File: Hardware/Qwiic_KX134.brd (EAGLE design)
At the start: 25.4 x 25.4 mm, 62 parts, among them J2 QWIIC, J4 QWIIC, U1 KX134

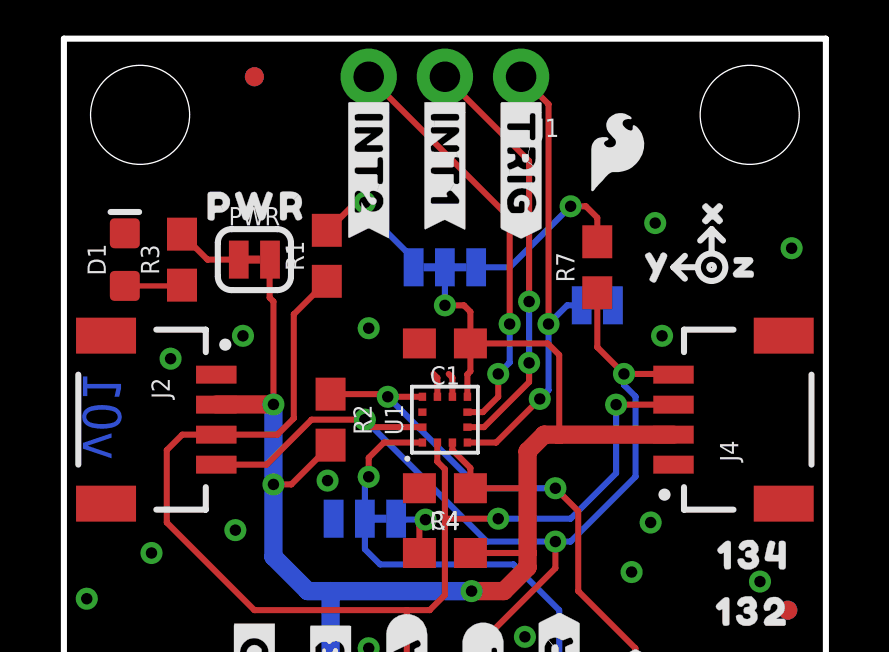
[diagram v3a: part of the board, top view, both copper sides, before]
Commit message: updating version number and orientation for review
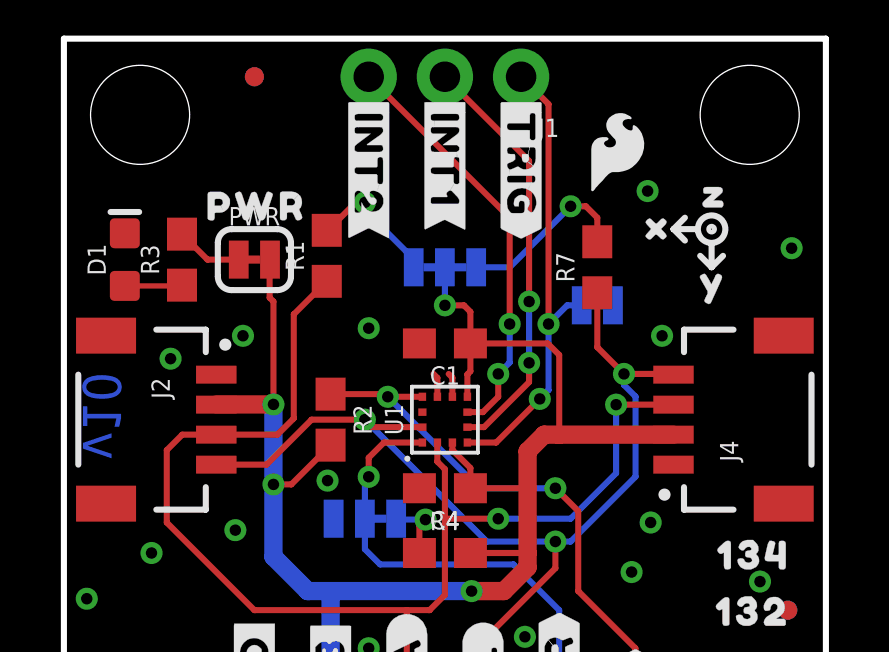
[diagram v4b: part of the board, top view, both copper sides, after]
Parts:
- moved U$21 2.77 mm to (22.6, 16.1)
- moved U$1 2.70 mm to (20.7, 17.9)
- moved U$30 2.55 mm to (20.6, 20.2)
- moved U$29 1.96 mm to (20.5, 17.3)
- moved U$28 1.95 mm to (18.7, 19.2)
- moved U$32 1.72 mm to (22.7, 19.1)
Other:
- board text added: "v10"
- board text removed: "v01"
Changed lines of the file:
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@@
 <wire x1="25.4" y1="25.4" x2="25.4" y2="0" width="0.2032" layer="20"/>
 <wire x1="25.4" y1="0" x2="0" y2="0" width="0.2032" layer="20"/>
-<text x="1.27" y="12.827" size="1.27" layer="16" font="vector" ratio="15" rot="MR90" align="center">v01</text>
+<text x="1.27" y="12.827" size="1.27" layer="16" font="vector" ratio="15" rot="MR90" align="center">v10</text>
 <dimension x1="0" y1="0" x2="0" y2="25.4" x3="-5.08" y3="12.7" textsize="1.778" textratio="15" layer="47" unit="inch"/>
 <dimension x1="2.54" y1="22.86" x2="2.54" y2="2.54" x3="-1.27" y3="12.7" textsize="1.778" textratio="15" layer="47" unit="inch"/>
@@
 <text x="12.7" y="35.56" size="1.778" layer="47" font="vector" ratio="15" align="center">Dimensions in inches</text>
 <text x="13.97" y="-7.62" size="1.778" layer="51" font="vector" ratio="10">Andy England</text>
-<wire x1="20.32" y1="17.78" x2="20.701" y2="18.161" width="0.2032" layer="21"/>
-<wire x1="20.32" y1="17.78" x2="20.701" y2="17.399" width="0.2032" layer="21"/>
-<wire x1="21.59" y1="18.288" x2="21.59" y2="19.05" width="0.2032" layer="21"/>
-<wire x1="21.59" y1="19.05" x2="21.971" y2="18.669" width="0.2032" layer="21"/>
-<wire x1="21.59" y1="19.05" x2="21.209" y2="18.669" width="0.2032" layer="21"/>
-<circle x="21.59" y="17.78" radius="0.457903125" width="0.2032" layer="21"/>
-<circle x="21.59" y="17.78" radius="0.0762" width="0.2032" layer="21"/>
-<wire x1="20.32" y1="17.78" x2="21.082" y2="17.78" width="0.2032" layer="21"/>
+<wire x1="21.59" y1="17.78" x2="21.209" y2="18.161" width="0.2032" layer="21"/>
+<wire x1="21.59" y1="17.78" x2="21.971" y2="18.161" width="0.2032" layer="21"/>
+<wire x1="21.082" y1="19.05" x2="20.32" y2="19.05" width="0.2032" layer="21"/>
+<wire x1="20.32" y1="19.05" x2="20.701" y2="19.431" width="0.2032" layer="21"/>
+<wire x1="20.32" y1="19.05" x2="20.701" y2="18.669" width="0.2032" layer="21"/>
+<circle x="21.59" y="19.05" radius="0.457903125" width="0.2032" layer="21"/>
+<circle x="21.59" y="19.05" radius="0.0762" width="0.2032" layer="21"/>
+<wire x1="21.59" y1="17.78" x2="21.59" y2="18.542" width="0.2032" layer="21"/>
+<wire x1="21.59" y1="16.51" x2="21.971" y2="16.891" width="0.2032" layer="22"/>
+<wire x1="21.59" y1="16.51" x2="21.209" y2="16.891" width="0.2032" layer="22"/>
+<wire x1="21.082" y1="17.78" x2="20.32" y2="17.78" width="0.2032" layer="22"/>
 <wire x1="20.32" y1="17.78" x2="20.701" y2="17.399" width="0.2032" layer="22"/>
 <wire x1="20.32" y1="17.78" x2="20.701" y2="18.161" width="0.2032" layer="22"/>
-<wire x1="21.59" y1="18.288" x2="21.59" y2="19.05" width="0.2032" layer="22"/>
-<wire x1="21.59" y1="19.05" x2="21.209" y2="18.669" width="0.2032" layer="22"/>
-<wire x1="21.59" y1="19.05" x2="21.971" y2="18.669" width="0.2032" layer="22"/>
 <circle x="21.59" y="17.78" radius="0.457903125" width="0.2032" layer="22"/>
-<wire x1="20.32" y1="17.78" x2="21.082" y2="17.78" width="0.2032" layer="22"/>
+<wire x1="21.59" y1="16.51" x2="21.59" y2="17.272" width="0.2032" layer="22"/>
+<wire x1="21.2725" y1="17.4625" x2="21.9075" y2="18.0975" width="0.2032" layer="22"/>
 <wire x1="21.2725" y1="18.0975" x2="21.9075" y2="17.4625" width="0.2032" layer="22"/>
-<wire x1="21.9075" y1="18.0975" x2="21.2725" y2="17.4625" width="0.2032" layer="22"/>
 <rectangle x1="20.5105" y1="7.62" x2="21.59" y2="8.6995" layer="29"/>
 <rectangle x1="20.5105" y1="5.7785" x2="21.59" y2="6.858" layer="29"/>
@@
 <element name="U$26" library="output" package="#SDO#0" value="" x="16.51" y="1.778" smashed="yes" rot="MR90"/>
 <element name="U$27" library="output" package="KX134_ACCELEROMETER0" value="" x="21.59" y="12.7" smashed="yes" rot="MR0"/>
-<element name="U$28" library="output" package="X0" value="" x="20.574" y="19.685" smashed="yes"/>
-<element name="U$29" library="output" package="Y0" value="" x="18.669" y="18.034" smashed="yes"/>
-<element name="U$30" library="output" package="Z0" value="" x="21.59" y="17.907" smashed="yes"/>
+<element name="U$28" library="output" package="X0" value="" x="18.6944" y="19.177" smashed="yes"/>
+<element name="U$29" library="output" package="Y0" value="" x="20.4978" y="17.3228" smashed="yes"/>
+<element name="U$30" library="output" package="Z0" value="" x="20.574" y="20.2438" smashed="yes"/>
 <element name="U$31" library="output" package="PWR0" value="" x="4.064" y="19.812" smashed="yes"/>
 <element name="R4" library="SparkFun-Resistors" package="0603" value="4.7k" x="12.7" y="8.255" smashed="yes">
@@
 <element name="U$17" library="output" package="#TRIG#2" value="" x="20.193" y="14.605" smashed="yes" rot="MR0"/>
 <element name="U$20" library="output" package="#ADR#3" value="" x="16.51" y="1.778" smashed="yes" rot="R90"/>
-<element name="U$1" library="output" package="X0" value="" x="22.6568" y="19.685" smashed="yes" rot="MR0"/>
-<element name="U$21" library="output" package="Y0" value="" x="20.701" y="18.034" smashed="yes" rot="MR0"/>
-<element name="U$32" library="output" package="Z0" value="" x="23.876" y="17.907" smashed="yes" rot="MR0"/>
+<element name="U$1" library="output" package="X0" value="" x="20.6756" y="17.8562" smashed="yes" rot="MR0"/>
+<element name="U$21" library="output" package="Y0" value="" x="22.6314" y="16.0528" smashed="yes" rot="MR0"/>
+<element name="U$32" library="output" package="Z0" value="" x="22.6568" y="19.1262" smashed="yes" rot="MR0"/>
 <element name="LOGO1" library="SparkFun-Aesthetics" package="SFE_LOGO_FLAME_.1" value="SFE_LOGO_FLAME.1_INCH" x="18.4404" y="21.6408" smashed="yes"/>
 <element name="LOGO2" library="SparkFun-Aesthetics" package="SFE_LOGO_FLAME_.1" value="SFE_LOGO_FLAME.1_INCH" x="18.3896" y="21.59" smashed="yes" rot="MR0"/>
@@
 <via x="5.715" y="9.017" extent="1-16" drill="0.381"/>
 <via x="0.762" y="6.731" extent="1-16" drill="0.381"/>
-<via x="19.7104" y="19.2532" extent="1-16" drill="0.381"/>
+<via x="19.4564" y="20.32" extent="1-16" drill="0.381"/>
 <contactref element="TRIG" pad="2"/>
 <contactref element="C1" pad="2"/>

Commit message: post design review, computer transfer
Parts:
- moved JP2 4.02 mm to (20.3, 5.08)
- moved JP5 4.02 mm to (20.3, 5.08)
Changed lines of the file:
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@@
 <element name="JP3" library="SparkFun" package="STAND-OFF" value="STAND-OFF" x="2.54" y="22.86" smashed="yes"/>
 <element name="JP4" library="SparkFun" package="STAND-OFF" value="STAND-OFF" x="22.86" y="22.86" smashed="yes"/>
-<element name="JP2" library="SparkFun" package="MICRO-FIDUCIAL" value="FIDUCIALUFIDUCIAL" x="24.13" y="6.35" smashed="yes"/>
+<element name="JP2" library="SparkFun" package="MICRO-FIDUCIAL" value="FIDUCIALUFIDUCIAL" x="20.32" y="5.08" smashed="yes"/>
 <element name="JP6" library="SparkFun" package="MICRO-FIDUCIAL" value="FIDUCIALUFIDUCIAL" x="6.35" y="24.13" smashed="yes"/>
 <element name="J2" library="SparkFun-Connectors" package="JST04_1MM_RA" value="QWIIC" x="5.08" y="12.7" smashed="yes" rot="R270">
@@
 </element>
 <element name="JP1" library="SparkFun" package="MICRO-FIDUCIAL" value="FIDUCIALUFIDUCIAL" x="6.35" y="24.13" smashed="yes" rot="MR0"/>
-<element name="JP5" library="SparkFun" package="MICRO-FIDUCIAL" value="FIDUCIALUFIDUCIAL" x="24.13" y="6.35" smashed="yes" rot="MR0"/>
+<element name="JP5" library="SparkFun" package="MICRO-FIDUCIAL" value="FIDUCIALUFIDUCIAL" x="20.32" y="5.08" smashed="yes" rot="MR0"/>
 <element name="R3" library="SparkFun-Resistors" package="0603" value="1k" x="3.937" y="18.034" smashed="yes" rot="R90">
 <attribute name="NAME" x="3.175" y="18.034" size="0.6096" layer="25" font="vector" ratio="20" rot="R90" align="bottom-center"/>

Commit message: post checklist changes
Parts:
- removed U$27: (no value), output:KX134_ACCELEROMETER0
- added LOGO3: QWIIC_LOGO_4MM, SparkFun-Aesthetics:QWIIC_4MM
- added LOGO4: SFE_LOGO_NAME_FLAME.1_INCH, SparkFun-Aesthetics:SFE_LOGO_NAME_FLAME_.1
- added U$16: (no value), buzzard_labels (1):KX13X_VIBRATION_SENSOR0
- U1: device KX134:KX134 -> SparkFun-Sensors:KX13X
- moved U$33 0.13 mm to (21.0, 6.43)
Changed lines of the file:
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@@
 <?xml version="1.0" encoding="utf-8"?>
 <!DOCTYPE eagle SYSTEM "eagle.dtd">
-<eagle version="9.6.0">
+<eagle version="9.6.2">
 <drawing>
 <settings>
@@
 <setting verticaltext="up"/>
 </settings>
-<grid distance="0.05" unitdist="inch" unit="inch" style="lines" multiple="1" display="yes" altdistance="0.002" altunitdist="inch" altunit="inch"/>
+<grid distance="0.05" unitdist="inch" unit="inch" style="lines" multiple="1" display="yes" altdistance="0.005" altunitdist="inch" altunit="inch"/>
 <layers>
 <layer number="1" name="Top" color="4" fill="1" visible="yes" active="yes"/>
@@
 <layer number="18" name="Vias" color="2" fill="1" visible="yes" active="yes"/>
 <layer number="19" name="Unrouted" color="6" fill="1" visible="yes" active="yes"/>
-<layer number="20" name="Dimension" color="15" fill="1" visible="yes" active="yes"/>
+<layer number="20" name="Dimension" color="24" fill="1" visible="yes" active="yes"/>
 <layer number="21" name="tPlace" color="16" fill="1" visible="yes" active="yes"/>
 <layer number="22" name="bPlace" color="14" fill="1" visible="yes" active="yes"/>
@@
 <layer number="28" name="bValues" color="7" fill="1" visible="no" active="yes"/>
 <layer number="29" name="tStop" color="7" fill="3" visible="yes" active="yes"/>
-<layer number="30" name="bStop" color="7" fill="6" visible="yes" active="yes"/>
+<layer number="30" name="bStop" color="7" fill="6" visible="no" active="yes"/>
 <layer number="31" name="tCream" color="7" fill="4" visible="yes" active="yes"/>
-<layer number="32" name="bCream" color="7" fill="5" visible="yes" active="yes"/>
-<layer number="33" name="tFinish" color="6" fill="3" visible="yes" active="yes"/>
-<layer number="34" name="bFinish" color="6" fill="6" visible="yes" active="yes"/>
-<layer number="35" name="tGlue" color="7" fill="4" visible="yes" active="yes"/>
-<layer number="36" name="bGlue" color="7" fill="5" visible="yes" active="yes"/>
-<layer number="37" name="tTest" color="7" fill="1" visible="yes" active="yes"/>
-<layer number="38" name="bTest" color="7" fill="1" visible="yes" active="yes"/>
-<layer number="39" name="tKeepout" color="4" fill="11" visible="yes" active="yes"/>
-<layer number="40" name="bKeepout" color="1" fill="11" visible="yes" active="yes"/>
-<layer number="41" name="tRestrict" color="4" fill="10" visible="yes" active="yes"/>
-<layer number="42" name="bRestrict" color="1" fill="10" visible="yes" active="yes"/>
-<layer number="43" name="vRestrict" color="2" fill="10" visible="yes" active="yes"/>
-<layer number="44" name="Drills" color="7" fill="1" visible="yes" active="yes"/>
+<layer number="32" name="bCream" color="7" fill="5" visible="no" active="yes"/>
+<layer number="33" name="tFinish" color="6" fill="3" visible="no" active="yes"/>
+<layer number="34" name="bFinish" color="6" fill="6" visible="no" active="yes"/>
+<layer number="35" name="tGlue" color="7" fill="4" visible="no" active="yes"/>
+<layer number="36" name="bGlue" color="7" fill="5" visible="no" active="yes"/>
+<layer number="37" name="tTest" color="7" fill="1" visible="no" active="yes"/>
+<layer number="38" name="bTest" color="7" fill="1" visible="no" active="yes"/>
+<layer number="39" name="tKeepout" color="4" fill="11" visible="no" active="yes"/>
+<layer number="40" name="bKeepout" color="1" fill="11" visible="no" active="yes"/>
+<layer number="41" name="tRestrict" color="4" fill="10" visible="no" active="yes"/>
+<layer number="42" name="bRestrict" color="1" fill="10" visible="no" active="yes"/>
+<layer number="43" name="vRestrict" color="2" fill="10" visible="no" active="yes"/>
+<layer number="44" name="Drills" color="7" fill="1" visible="no" active="yes"/>
 <layer number="45" name="Holes" color="7" fill="1" visible="yes" active="yes"/>
-<layer number="46" name="Milling" color="3" fill="1" visible="yes" active="yes"/>
+<layer number="46" name="Milling" color="3" fill="1" visible="no" active="yes"/>
 <layer number="47" name="Measures" color="7" fill="1" visible="yes" active="yes"/>
-<layer number="48" name="Document" color="7" fill="1" visible="yes" active="yes"/>
-<layer number="49" name="Reference" color="7" fill="1" visible="yes" active="yes"/>
-<layer number="50" name="dxf" color="7" fill="1" visible="yes" active="yes"/>
+<layer number="48" name="Document" color="7" fill="1" visible="no" active="yes"/>
+<layer number="49" name="Reference" color="7" fill="1" visible="no" active="yes"/>
+<layer number="50" name="dxf" color="7" fill="1" visible="no" active="yes"/>
 <layer number="51" name="tDocu" color="6" fill="1" visible="yes" active="yes"/>
-<layer number="52" name="bDocu" color="7" fill="1" visible="yes" active="yes"/>
+<layer number="52" name="bDocu" color="7" fill="1" visible="no" active="yes"/>
 <layer number="91" name="Nets" color="2" fill="1" visible="no" active="no"/>
 <layer number="92" name="Busses" color="1" fill="1" visible="no" active="no"/>
@@
 <wire x1="21.2725" y1="17.4625" x2="21.9075" y2="18.0975" width="0.2032" layer="22"/>
 <wire x1="21.2725" y1="18.0975" x2="21.9075" y2="17.4625" width="0.2032" layer="22"/>
-<rectangle x1="20.5105" y1="7.62" x2="21.59" y2="8.6995" layer="29"/>
-<rectangle x1="20.5105" y1="5.7785" x2="21.59" y2="6.858" layer="29"/>
-<rectangle x1="20.5105" y1="5.7785" x2="21.59" y2="6.858" layer="31"/>
+<rectangle x1="20.5105" y1="7.62" x2="20.955" y2="8.6995" layer="29"/>
+<rectangle x1="20.3835" y1="7.5565" x2="21.6535" y2="8.763" layer="31"/>
+<rectangle x1="21.1455" y1="7.62" x2="21.59" y2="8.6995" layer="29"/>
+<rectangle x1="20.5105" y1="5.842" x2="20.955" y2="6.9215" layer="29"/>
+<rectangle x1="20.3835" y1="5.7785" x2="21.6535" y2="6.985" layer="31"/>
+<rectangle x1="21.1455" y1="5.842" x2="21.59" y2="6.9215" layer="29"/>
 </plain>
 <attributes>
@@
 <element name="U$25" library="output" package="#SCLK#0" value="" x="13.97" y="1.778" smashed="yes" rot="MR90"/>
 <element name="U$26" library="output" package="#SDO#0" value="" x="16.51" y="1.778" smashed="yes" rot="MR90"/>
-<element name="U$27" library="output" package="KX134_ACCELEROMETER0" value="" x="21.59" y="12.7" smashed="yes" rot="MR0"/>
 <element name="U$28" library="output" package="X0" value="" x="18.6944" y="19.177" smashed="yes"/>
 <element name="U$29" library="output" package="Y0" value="" x="20.4978" y="17.3228" smashed="yes"/>
@@
 <attribute name="VALUE" x="5.08" y="-0.762" size="0.6096" layer="27" font="vector" ratio="20"/>
 </element>
-<element name="U1" library="KX134" package="KX134" value="KX134" x="12.7" y="12.7" smashed="yes" rot="R90">
+<element name="U1" library="SparkFun-Sensors" package="KX13X" value="KX134" x="12.7" y="12.7" smashed="yes" rot="R90">
 <attribute name="NAME" x="11" y="12.7" size="0.6096" layer="25" font="vector" ratio="20" rot="R90" align="center"/>
 <attribute name="PROD_ID" value="IC-15486" x="12.7" y="12.7" size="1.778" layer="27" rot="R90" display="off"/>
@@
 <element name="LOGO1" library="SparkFun-Aesthetics" package="SFE_LOGO_FLAME_.1" value="SFE_LOGO_FLAME.1_INCH" x="18.4404" y="21.6408" smashed="yes"/>
 <element name="LOGO2" library="SparkFun-Aesthetics" package="SFE_LOGO_FLAME_.1" value="SFE_LOGO_FLAME.1_INCH" x="18.3896" y="21.59" smashed="yes" rot="MR0"/>
-<element name="U$33" library="output" package="1320" value="" x="21.0312" y="6.2992" smashed="yes"/>
+<element name="U$33" library="output" package="1320" value="" x="21.0312" y="6.4262" smashed="yes"/>
 <element name="U$34" library="output" package="1340" value="" x="21.082" y="8.1788" smashed="yes"/>
+<element name="U$16" library="buzzard_labels (1)" package="KX13X_VIBRATION_SENSOR0" value="" x="21.844" y="12.7" smashed="yes" rot="MR0"/>
+<element name="LOGO3" library="SparkFun-Aesthetics" package="QWIIC_4MM" value="QWIIC_LOGO_4MM" x="2.54" y="7.62" smashed="yes"/>
+<element name="LOGO4" library="SparkFun-Aesthetics" package="SFE_LOGO_NAME_FLAME_.1" value="SFE_LOGO_NAME_FLAME.1_INCH" x="-31.75" y="-15.24" smashed="yes"/>
 </elements>
 <signals>
